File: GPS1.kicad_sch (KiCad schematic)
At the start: 1 part, among them J3 Conn_01x05_Pin

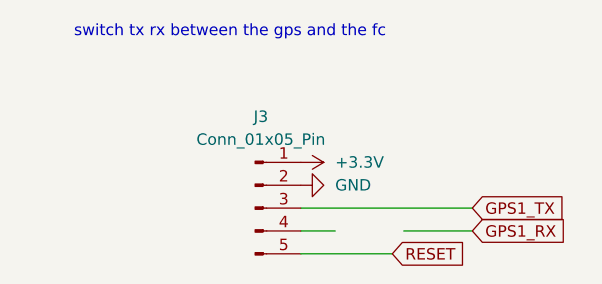
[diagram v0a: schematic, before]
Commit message: began fixing schematic added barometer
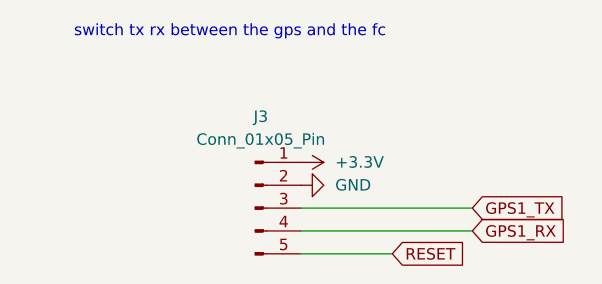
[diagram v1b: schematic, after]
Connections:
- net GPS1_RX: now also J3.4 (Pin_4)
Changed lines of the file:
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@@
 	(wire
 		(pts
-			(xy 111.76 73.66) (xy 107.95 73.66)
+			(xy 107.95 73.66) (xy 127 73.66)
 		)
 		(stroke
-			(width 0)
-			(type default)
-		)
-	)
-	(wire
-		(pts
-			(xy 127 73.66) (xy 119.38 73.66)
-		)
-		(stroke
